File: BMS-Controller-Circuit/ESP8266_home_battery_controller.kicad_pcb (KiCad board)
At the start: 2 copper layers, 45 x 65 mm, 33 parts, among them J1 I2C, J2 Battery Bank, J3 Charge Ctl, J4 Inv Power, J5 , J6 , J7 , J8 , J9 Charger Relay, U1 WeMos_mini, U2 AD5242BRUZ10, U3 MAX5033AASA, U4 INA226

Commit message: ESP8266 Controller PCB Ver 0.2
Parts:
- added C5: 100 nF, Capacitor_SMD:C_1206_3216Metric_Pad1.42x1.75mm_HandSolder, F.Cu at (185.0, 105.0)
- J1: value I2C -> I2C to diyBMS
- J3: value Charge Ctl -> Charger Voltage Ctl
- J4: value Inv Power -> Inverter Power Ctl
- L1: footprint Inductors_SMD:L_7.3x7.3_H3.5 -> Inductor_SMD:L_Bourns_SRN6045TA
- moved R7 2.00 mm to (181.0, 104.4)
- moved R4 1.00 mm to (185.0, 65.0)
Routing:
- net GND: track 243.3 -> 246.6 mm, vias 9 -> 10
- net Net-(J2-Pad2): track 24.8 -> 22.8 mm
- net Net-(R4-Pad2): track 12.4 -> 13.4 mm
- net Net-(J3-Pad1): track 4.55 -> 3.55 mm
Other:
- board text added: "Battery Shunt"
- board text added: "Charger"
- board text added: "I2C"
- board text added: "Inverter"
- board text added: "Relays"
- board text added: "diyBMS Controller Derek Jennings Oct'18 v 0.2"
- board text removed: "diyBMS Controller Derek Jennings Oct'18 v 0.1"

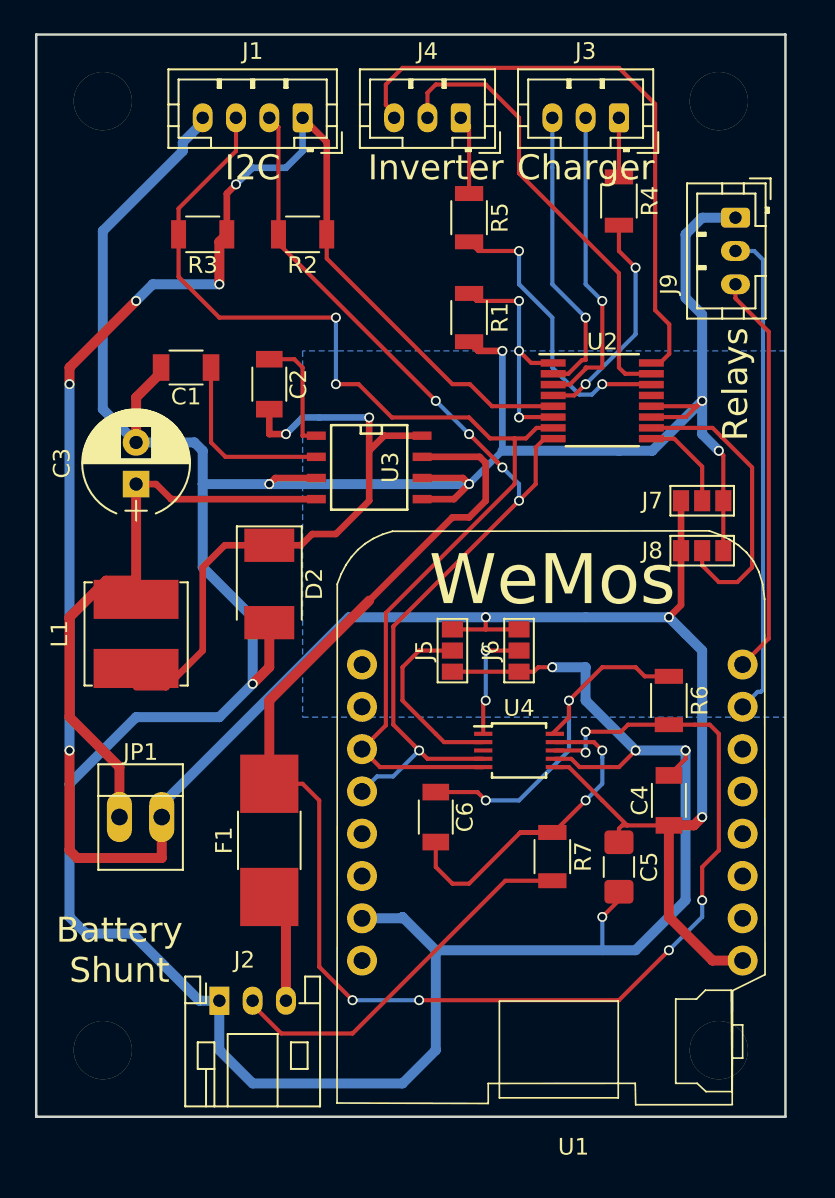
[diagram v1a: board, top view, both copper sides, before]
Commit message: Update Controller PCB * Remove digitots * Add serial interface
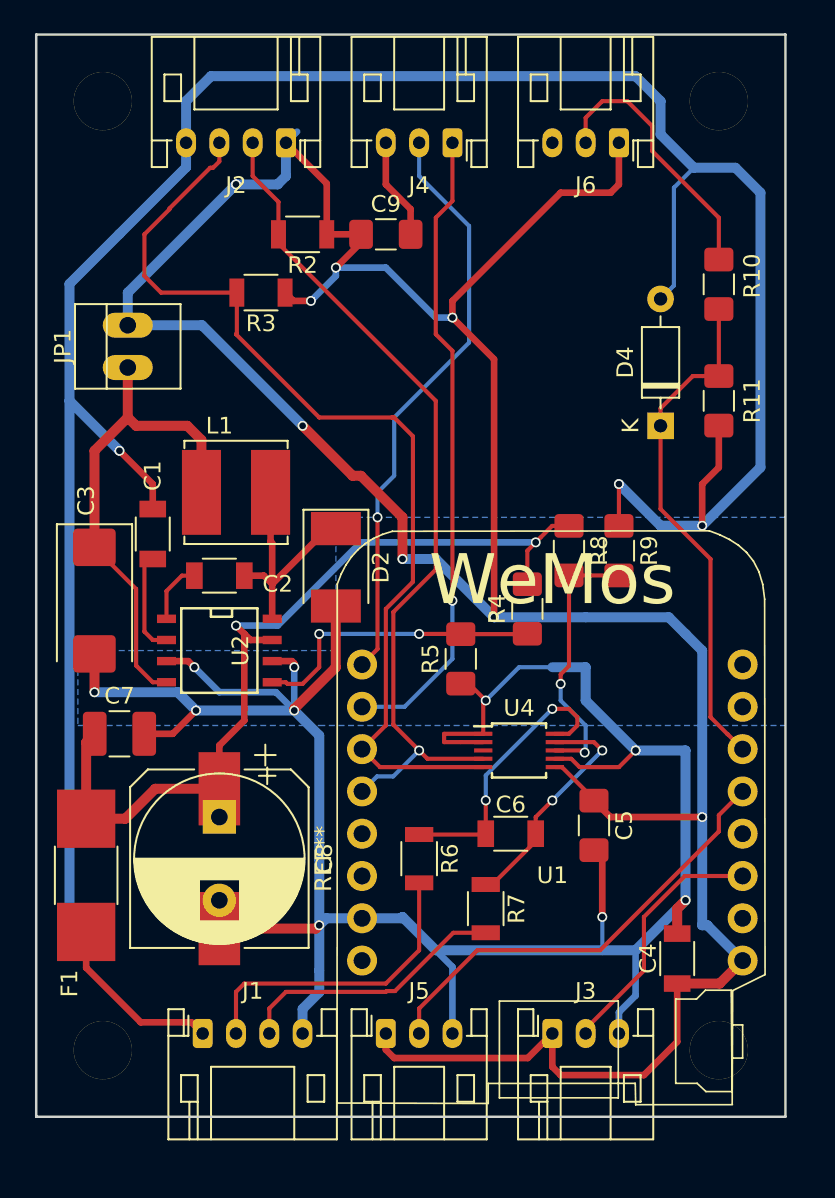
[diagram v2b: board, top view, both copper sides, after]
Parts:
- removed J7, J8: , Connectors:GS3
- removed J9: Charger Relay, Connector_JST:JST_PH_B3B-PH-K_1x03_P2.00mm_Vertical
- removed R1: 10K, Resistors_SMD:R_1206
- removed the U2 at (184.0, 77.0)
- added C7: 1 uF 100V, Capacitor_SMD:C_1210_3225Metric_Pad1.42x2.65mm_HandSolder, F.Cu at (155.0, 97.0)
- added C8: 47uF, Capacitor_SMD:CP_Elec_10x14.3, F.Cu at (161.0, 104.5)
- added C9: 100 nF, Capacitor_SMD:C_1206_3216Metric_Pad1.42x1.75mm_HandSolder, F.Cu at (171.0, 67.0)
- added D4: 3.0V, Diode_THT:D_DO-35_SOD27_P7.62mm_Horizontal, F.Cu at (187.5, 78.5)
- added R10: 4K7, Resistor_SMD:R_1206_3216Metric_Pad1.42x1.75mm_HandSolder, F.Cu at (191.0, 70.0)
- added R11: 5K6, Resistor_SMD:R_1206_3216Metric_Pad1.42x1.75mm_HandSolder, F.Cu at (191.0, 77.0)
- added R8: 100K, Resistor_SMD:R_1206_3216Metric_Pad1.42x1.75mm_HandSolder, F.Cu at (182.0, 86.0)
- added R9: 100K, Resistor_SMD:R_1206_3216Metric_Pad1.42x1.75mm_HandSolder, F.Cu at (185.0, 86.0)
- added REF**: CP_Radial_D10.0mm_P5.00mm, Capacitor_THT:CP_Radial_D10.0mm_P5.00mm, F.Cu at (161.0, 102.0)
- C3: value 33uF -> 47uF Vishay TR3D476K016C0200; footprint Capacitors_THT:CP_Radial_D6.3mm_P2.50mm -> Capacitor_Tantalum_SMD:CP_EIA-7343-31_Kemet-D_Pad2.25x2.55mm_HandSolder
- D2: value SS110B -> CD214A-B360LF
- F1: value 50mA -> 85mA
- J1: value I2C to diyBMS -> Battery/Shunt; footprint Connector_JST:JST_PH_B4B-PH-K_1x04_P2.00mm_Vertical -> Connector_JST:JST_PH_S4B-PH-K_1x04_P2.00mm_Horizontal
- J2: value Battery Bank -> I2C; footprint Connectors_JST:JST_PH_S3B-PH-K_03x2.00mm_Angled -> Connector_JST:JST_PH_S4B-PH-K_1x04_P2.00mm_Horizontal
- J3: value Charger Voltage Ctl -> Inverter Relay; footprint Connector_JST:JST_PH_B3B-PH-K_1x03_P2.00mm_Vertical -> Connector_JST:JST_PH_S3B-PH-K_1x03_P2.00mm_Horizontal
- J4: value Inverter Power Ctl -> BST900 Serial; footprint Connector_JST:JST_PH_B3B-PH-K_1x03_P2.00mm_Vertical -> Connector_JST:JST_PH_S3B-PH-K_1x03_P2.00mm_Horizontal
- J5: value (none) -> Charger Relay; footprint Connectors:GS3 -> Connector_JST:JST_PH_S3B-PH-K_1x03_P2.00mm_Horizontal
- J6: value (none) -> Smoke Alarm; footprint Connectors:GS3 -> Connector_JST:JST_PH_S3B-PH-K_1x03_P2.00mm_Horizontal
- L1: value 220uH -> 150uH
- R4: value 0R -> 1M; footprint Resistors_SMD:R_1206 -> Resistor_SMD:R_1206_3216Metric_Pad1.42x1.75mm_HandSolder
- R5: value 0R -> 390K; footprint Resistors_SMD:R_1206 -> Resistor_SMD:R_1206_3216Metric_Pad1.42x1.75mm_HandSolder
- moved J1 55.3 mm to (160.0, 115.0), turned to 0 degrees
- moved J3 55.1 mm to (181.0, 115.0), turned to 0 degrees
- moved J2 51.7 mm to (165.0, 61.5), turned to 180 degrees
- moved J6 31.1 mm to (185.0, 61.5), turned to 180 degrees
- moved JP1 27.0 mm to (155.5, 75.0), turned to 90 degrees
- moved R5 26.5 mm to (175.5, 92.5), turned to 90 degrees
- moved R4 25.1 mm to (179.5, 89.5), turned to 90 degrees
- moved J5 23.3 mm to (171.0, 115.0)
- moved R6 17.8 mm to (173.0, 104.5)
- moved U2 14.2 mm to (161.0, 92.0)
- moved C2 11.9 mm to (161.0, 87.5), turned to 0 degrees
- moved F1 11.2 mm to (153.0, 105.5)
- moved L1 10.4 mm to (162.0, 82.5), turned to 180 degrees
- moved C1 10.2 mm to (157.0, 85.0), turned to 90 degrees
- moved C4 9.51 mm to (188.5, 110.5)
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- renumbered U3 to U2
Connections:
- J1 pad 1: +3V3 -> Net-(F1-Pad1)
- J1 pad 2: /SDA -> Net-(J1-Pad2)
- J1 pad 3: /SCL -> Net-(J1-Pad3)
- J2 pad 1: GND -> +3V3
- J2 pad 2: Net-(J2-Pad2) -> /SDA
- J2 pad 3: Net-(F1-Pad1) -> /SCL
- J3 pad 1: Net-(J3-Pad1) -> +3V3
- J3 pad 3: Net-(J3-Pad3) -> GND
- J4 pad 3: Net-(J4-Pad3) -> GND
- R4 pad 1: Net-(J3-Pad1) -> Net-(R4-Pad1)
- R4 pad 2: Net-(R4-Pad2) -> +BATT
- R5 pad 1: Net-(J4-Pad1) -> GND
- R5 pad 2: Net-(R5-Pad2) -> Net-(R4-Pad1)
- R6 pad 2: +BATT -> Net-(J1-Pad2)
- R7 pad 2: Net-(J2-Pad2) -> Net-(J1-Pad3)
- U1 pad 12: Net-(U1-Pad12) -> Net-(J5-Pad2)
- U1 pad 14: Net-(U1-Pad14) -> Net-(J3-Pad2)
- U1 pad 7: Net-(U1-Pad7) -> Net-(J4-Pad1)
- U1 pad 8: Net-(U1-Pad8) -> Net-(J4-Pad2)
- U2 pad 5: GND -> Net-(R4-Pad1)
- U4 pad 1: Net-(J6-Pad2) -> GND
- U4 pad 2: Net-(J5-Pad2) -> GND
- U4 pad 8: +BATT -> Net-(R8-Pad2)
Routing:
- net GND: track 246.6 -> 301.3 mm, vias 10 -> 13
- net +BATT: track 91.6 -> 52.1 mm, vias 6 -> 2
- net Net-(J4-Pad3): track 36.4 -> 0.00 mm
- net Net-(J4-Pad1): track 4.76 -> 38.5 mm, vias 0 -> 1
- net Net-(D4-Pad1): track 0.00 -> 30.8 mm
- net Net-(U1-Pad10): track 29.3 -> 0.00 mm
- net Net-(U1-Pad9): track 24.3 -> 0.00 mm
- net Net-(C2-Pad2): track 38.3 -> 14.7 mm, vias 2 -> 0
- net Net-(J2-Pad2): track 22.8 -> 0.00 mm
- net Net-(J1-Pad2): track 0.00 -> 18.6 mm
- net Net-(R5-Pad2): track 18.0 -> 0.00 mm, vias 2 -> 0
- net Net-(R4-Pad1): track 0.00 -> 17.8 mm, vias 0 -> 2
- net Net-(J8-Pad2): track 17.7 -> 0.00 mm
- net Net-(J3-Pad3): track 17.7 -> 0.00 mm, vias 1 -> 0
- net Net-(J1-Pad3): track 0.00 -> 16.4 mm
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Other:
- board text added: "Battery/Shunt"
- board text added: "Charge Relay"
- board text added: "Invert Relay"
- board text added: "Serial"
- board text added: "Smoke Detect"
- board text added: "diyBMS Controller Derek Jennings Apr'19 v 0.6"
- board text removed: "Battery Shunt"
- board text removed: "Charger"
- board text removed: "Inverter"
- board text removed: "Relays"
- board text removed: "diyBMS Controller Derek Jennings Oct'18 v 0.2"
